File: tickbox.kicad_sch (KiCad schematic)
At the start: 5 parts, among them IC1 R5F10RLAGFB#10, Y1 32.768 kHz

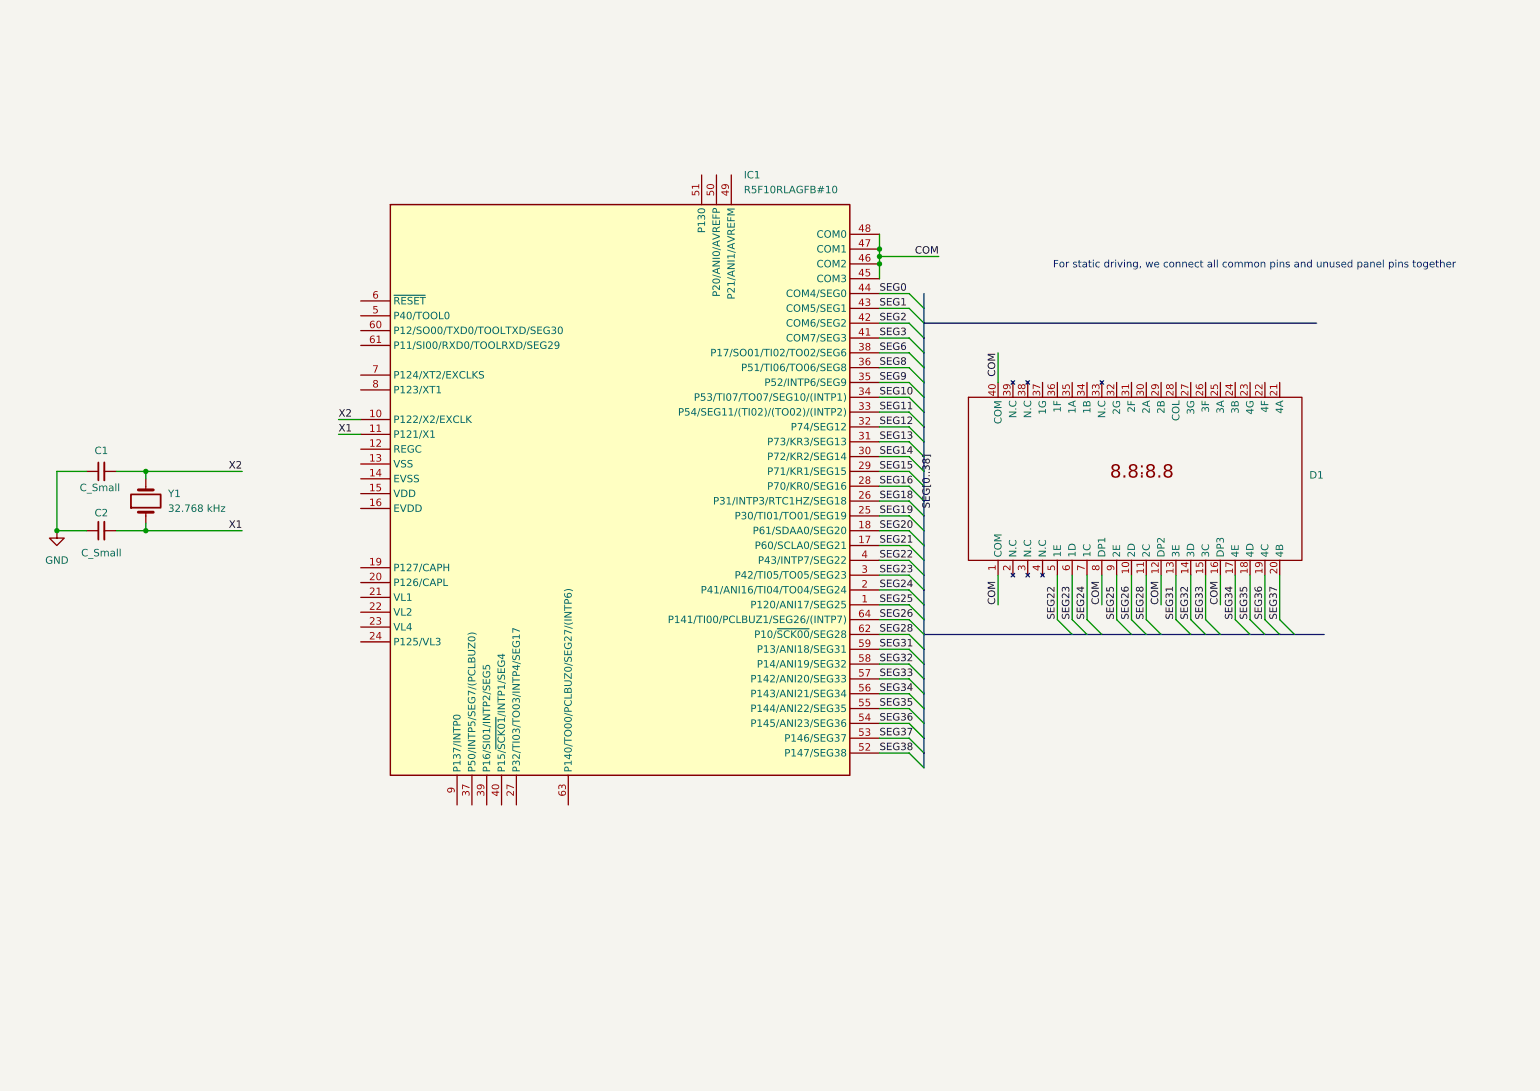
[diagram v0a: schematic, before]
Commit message: add rpi programming header
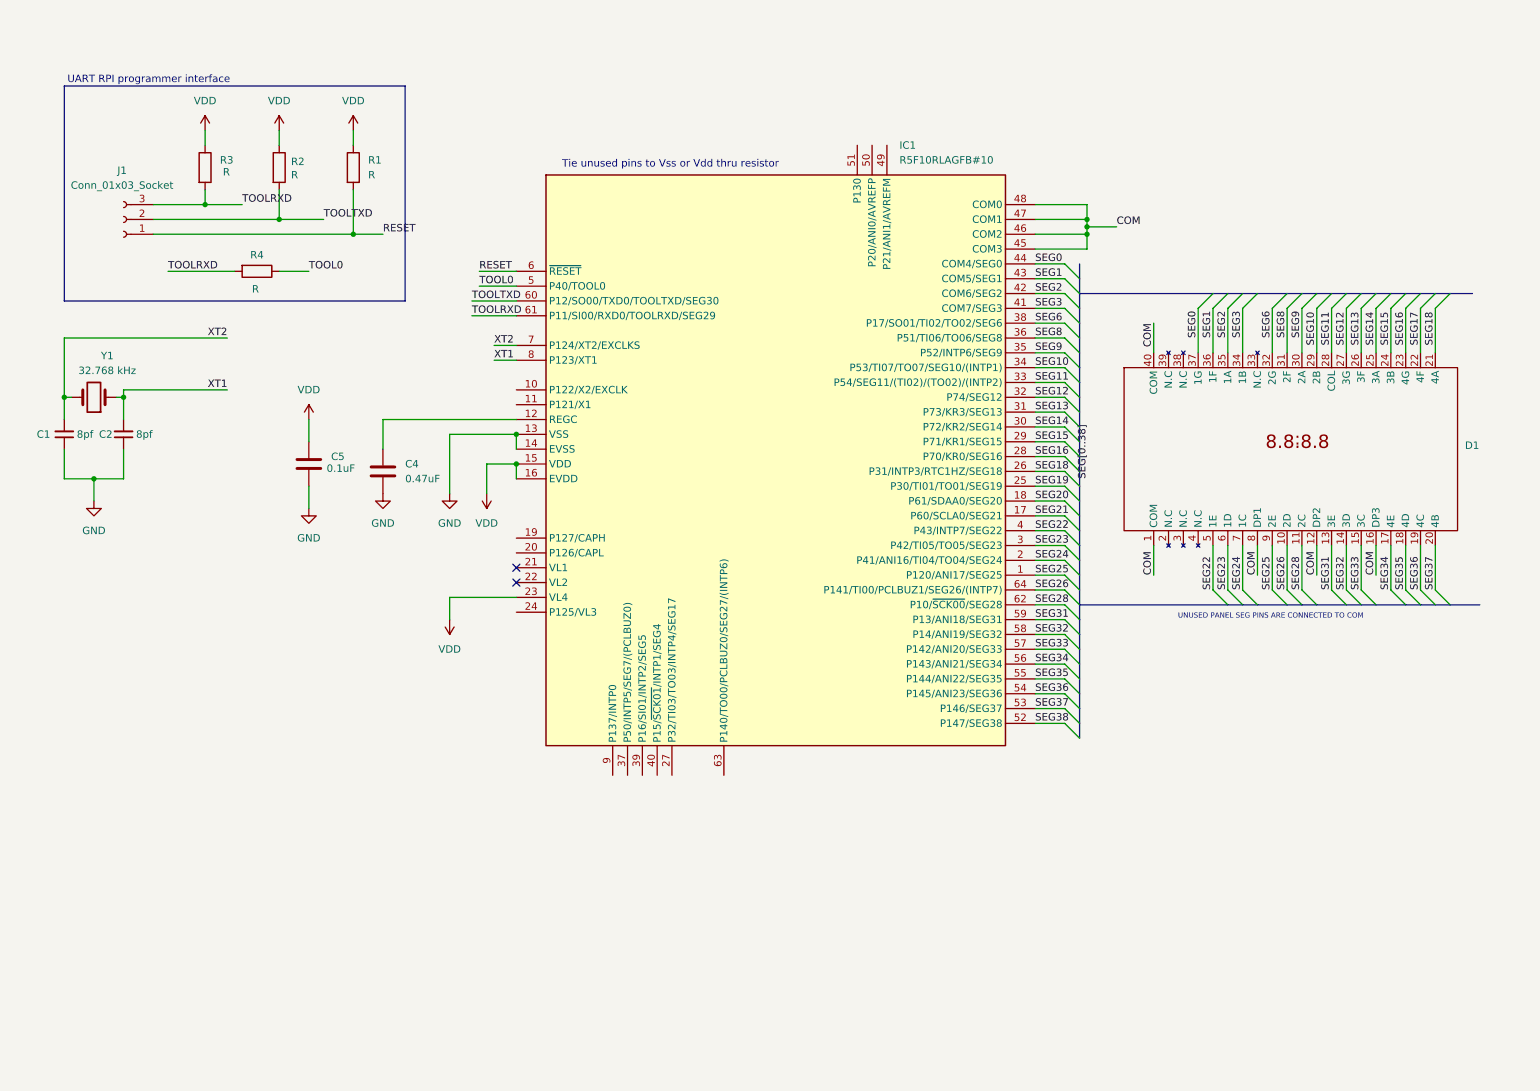
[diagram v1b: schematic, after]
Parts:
- added C4: 0.47uF, symbol Device:C
- added C5: 0.1uF, symbol Device:C
- added J1: Conn_01x03_Socket, symbol Connector:Conn_01x03_Socket
- added R1, R2, R3, R4: R, symbol Device:R
- C1, C2: value C_Small -> 8pf
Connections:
- net GND: now also IC1.13 (VSS), IC1.14 (EVSS), C4.2, C5.2
- net SEG0: now also D1.37 (1G)
- net SEG1: now also D1.36 (1F)
- net SEG10: now also D1.29 (2B)
- net SEG11: now also D1.28 (COL)
- net SEG12: now also D1.27 (3G)
- net SEG13: now also D1.26 (3F)
- net SEG14: now also D1.25 (3A)
- net SEG15: now also D1.24 (3B)
- net SEG16: now also D1.23 (4G)
- net SEG18: now also D1.21 (4A)
- net SEG2: now also D1.35 (1A)
- net SEG3: now also D1.34 (1B)
- net SEG6: now also D1.32 (2G)
- net SEG8: now also D1.31 (2F)
- net SEG9: now also D1.30 (2A)
- net at IC1.12 (REGC): now also C4.1
- net VDD: now reaches IC1.15 (VDD)
- net VDD: now also IC1.16 (EVDD), IC1.23 (VL4), C5.1, R1.1, R2.1, R3.1
- net TOOL0: now reaches IC1.5 (P40/TOOL0)
- net TOOL0: now also R4.1
- net RESET: now reaches IC1.6 (~{RESET})
- net RESET: now also J1.1 (Pin_1), R1.2
- net TOOLTXD: now reaches IC1.60 (P12/SO00/TXD0/TOOLTXD/SEG30)
- net TOOLTXD: now also J1.2 (Pin_2), R2.2
- net TOOLRXD: now reaches IC1.61 (P11/SI00/RXD0/TOOLRXD/SEG29)
- net TOOLRXD: now also J1.3 (Pin_3), R3.2, R4.2
- net XT2: now reaches IC1.7 (P124/XT2/EXCLKS)
- net XT2: now also C1.2, Y1.2
- net XT1: now reaches IC1.8 (P123/XT1)
- net XT1: now also C2.2, Y1.1
- net SEG17: now reaches D1.22 (4F)
- removed net X1: C2.2, IC1.11 (P121/X1), Y1.1
- removed net X2: C1.2, IC1.10 (P122/X2/EXCLK), Y1.2
- no-connect marks 0 -> 2
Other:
- note added: "Tie unused pins to Vss or Vdd thru resistor"
- note added: "UART RPI programmer interface"
- note added: "UNUSED PANEL SEG PINS ARE CONNECTED TO COM"
- note removed: "For static driving, we connect all common pins and unused panel pins together"
- moved on the sheet: C1, C2, D1, IC1, Y1

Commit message: Added LCD pads footprint
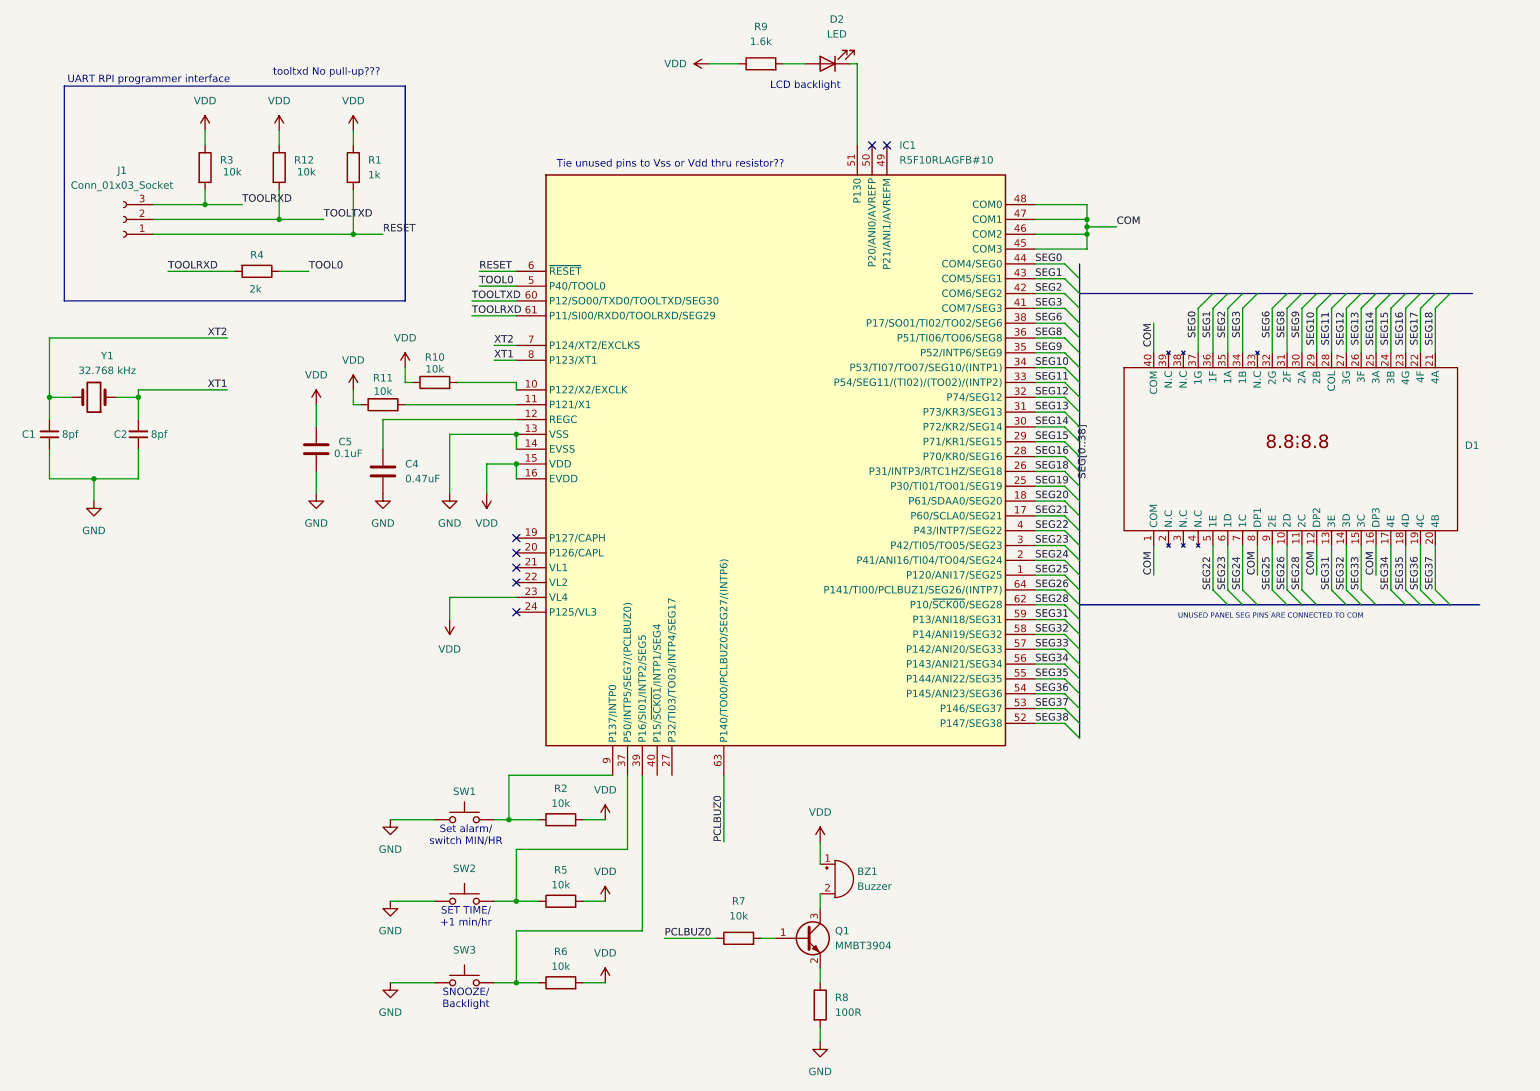
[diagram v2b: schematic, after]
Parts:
- added BZ1: Buzzer, symbol Device:Buzzer
- added D2: LED, symbol Device:LED
- added Q1: MMBT3904, Package_TO_SOT_SMD:SOT-23, symbol Transistor_BJT:MMBT3904
- added R10, R11, R12, R5, R6, R7: 10k, symbol Device:R
- added R8: 100R, symbol Device:R
- added R9: 1.6k, symbol Device:R
- added SW1, SW2, SW3: SW_MEC_5G, symbol Switch:SW_MEC_5G
- D1: footprint (none) -> 3rdparty:VI-402
- IC1: footprint QFP50P1200X1200X170-64M -> 3rdparty:QFP50P1200X1200X170-64M
- R1: value R -> 1k
- R2, R3: value R -> 10k
- R4: value R -> 2k
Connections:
- net GND: now also R8.2, SW1.1 (A), SW1.2 (A), SW2.1 (A), SW2.2 (A), SW3.1 (A), SW3.2 (A)
- net TOOLTXD: now also R12.2; no longer R2.2
- net VDD: now also R2.2, BZ1.1 (+), R10.1, R11.1, R12.1, R5.2, R6.2, R9.1; no longer R2.1
- net at IC1.10 (P122/X2/EXCLK): now also R10.2
- net at IC1.11 (P121/X1): now also R11.2
- net at IC1.37 (P50/INTP5/SEG7/(PCLBUZ0)): now also R5.1, SW2.3 (B), SW2.4 (B)
- net at IC1.39 (P16/SI01/INTP2/SEG5): now also R6.1, SW3.3 (B), SW3.4 (B)
- net at IC1.51 (P130): now also D2.1 (K)
- net PCLBUZ0: now reaches IC1.63 (P140/TO00/PCLBUZ0/SEG27/(INTP6))
- net PCLBUZ0: now also R7.1
- net at IC1.9 (P137/INTP0): now also R2.1, SW1.3 (B), SW1.4 (B)
- new net: Q1.1 (B), R7.2
- new net: Q1.2 (E), R8.1
- new net: BZ1.2 (-), Q1.3 (C)
- new net: D2.2 (A), R9.2
- no-connect marks 2 -> 7
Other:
- note added: "LCD backlight"
- note added: "SET TIME/ +1 min/hr"
- note added: "SNOOZE/ Backlight"
- note added: "Set alarm/ switch MIN/HR"
- note added: "Tie unused pins to Vss or Vdd thru resistor??"
- note added: "tooltxd No pull-up???"
- note removed: "Tie unused pins to Vss or Vdd thru resistor"
- moved on the sheet: C1, C2, C5

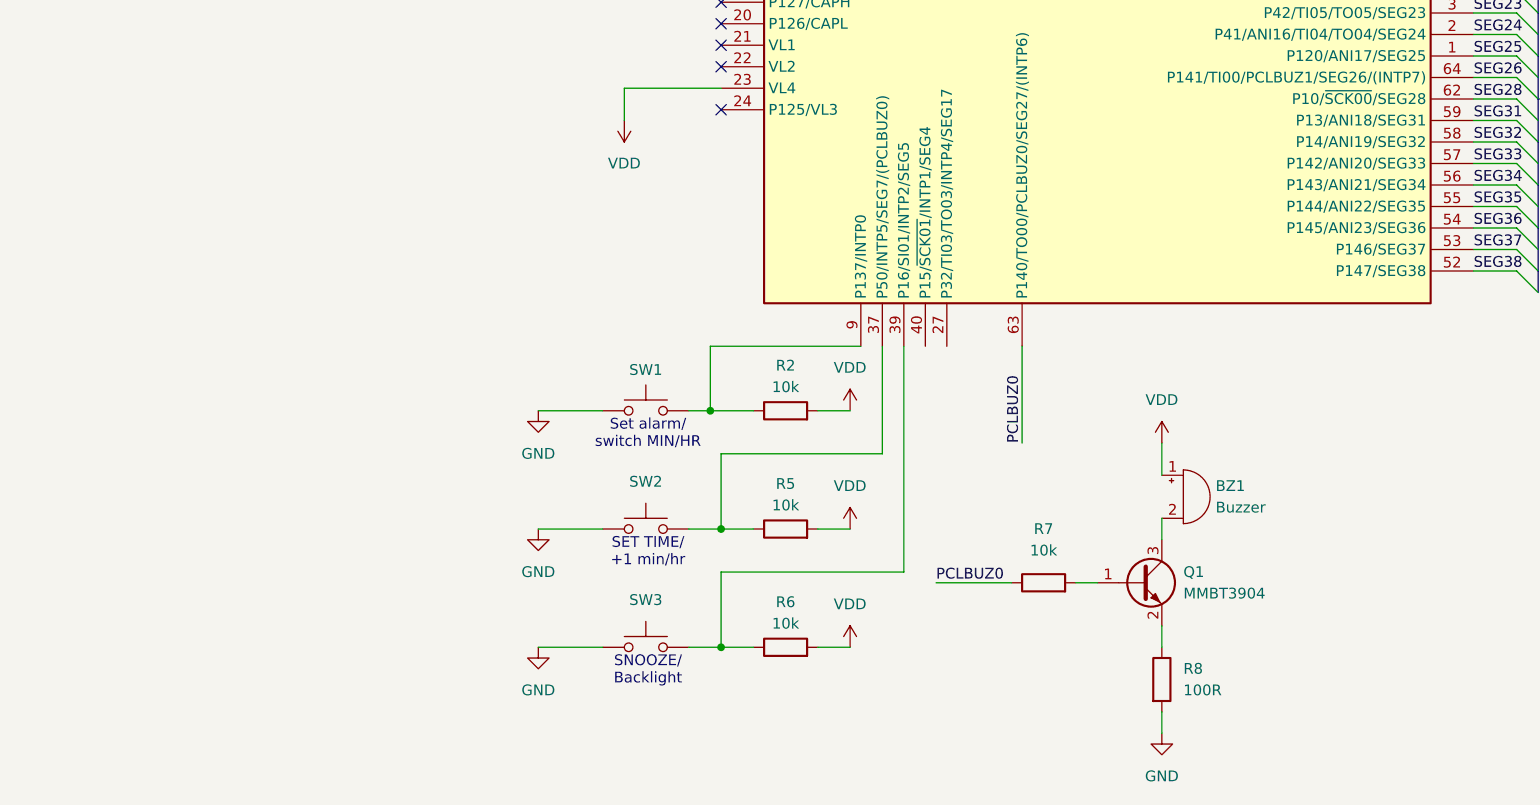
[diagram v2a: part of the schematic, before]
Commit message: Assing footprints + slight changes to schematic
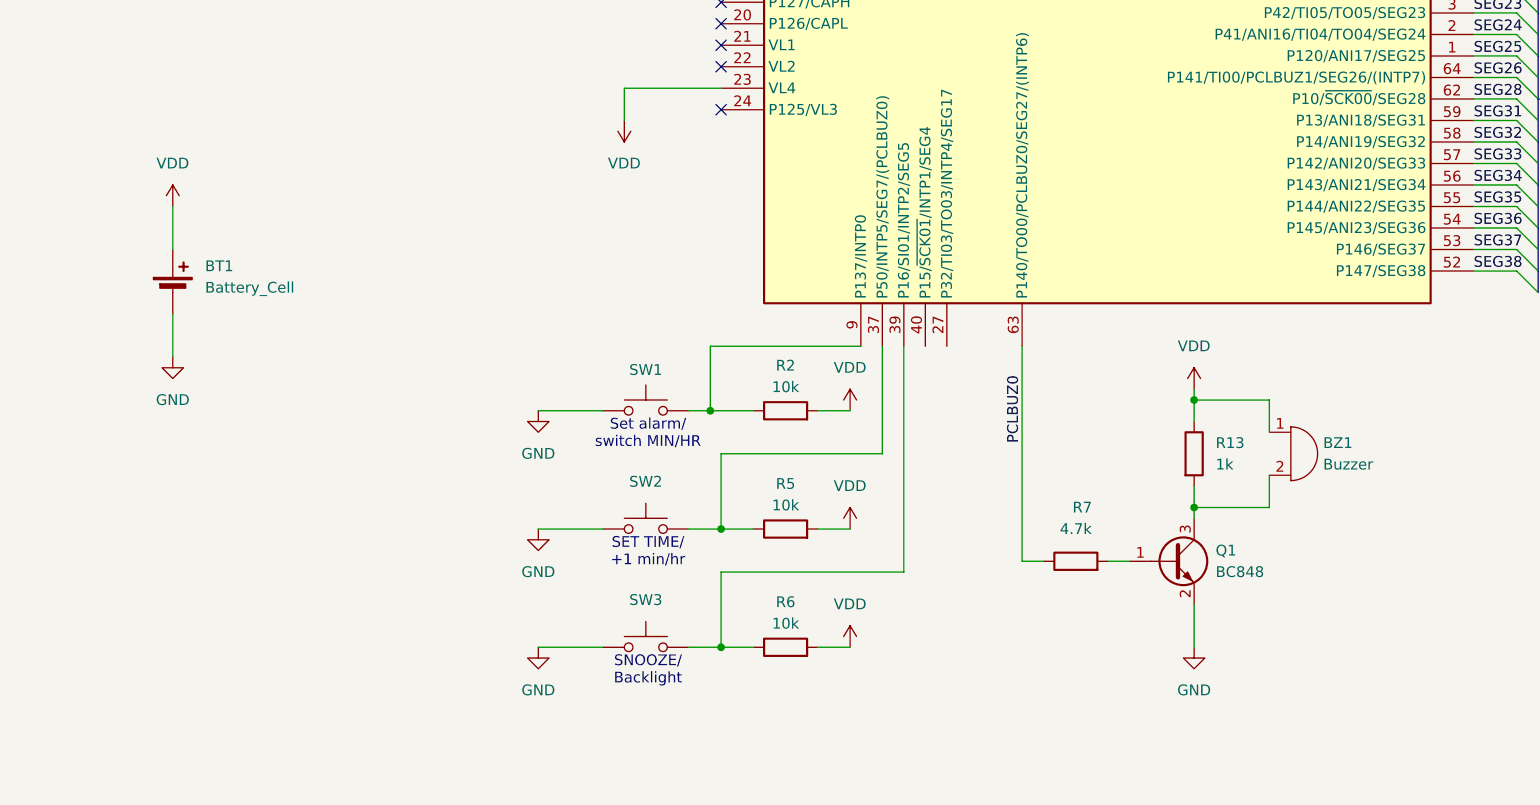
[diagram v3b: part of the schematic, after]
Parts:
- removed Q1: MMBT3904, Package_TO_SOT_SMD:SOT-23, symbol Transistor_BJT:MMBT3904
- removed R8: 100R, symbol Device:R
- added BT1: Battery_Cell, 3rdparty:COIN_HOLDER_TH, symbol Device:Battery_Cell
- added Q1: BC848, Package_TO_SOT_SMD:SOT-23, symbol Transistor_BJT:BC848
- added R13: 1k, symbol Device:R
- R7: value 10k -> 4.7k
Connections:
- net GND: now also BT1.2 (-), Q1.2 (E)
- net VDD: now also BT1.1 (+), R13.1
- net at R7.2: now also Q1.1 (B)
- net at BZ1.2 (-): now also Q1.3 (C), R13.2
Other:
- moved on the sheet: R7
